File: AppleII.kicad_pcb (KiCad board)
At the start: 2 copper layers, 215.5 x 361.2 mm, 201 parts, among them J0 Cassette Data In, J1 74LS257, J13 74LS74, J14 GAME_IO_Conn, J18 Aux Video, J2 Cassette Data Out, J3 Conn_01x16, J4 Conn_01x25, J5 Conn_01x25, J6 Conn_01x24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

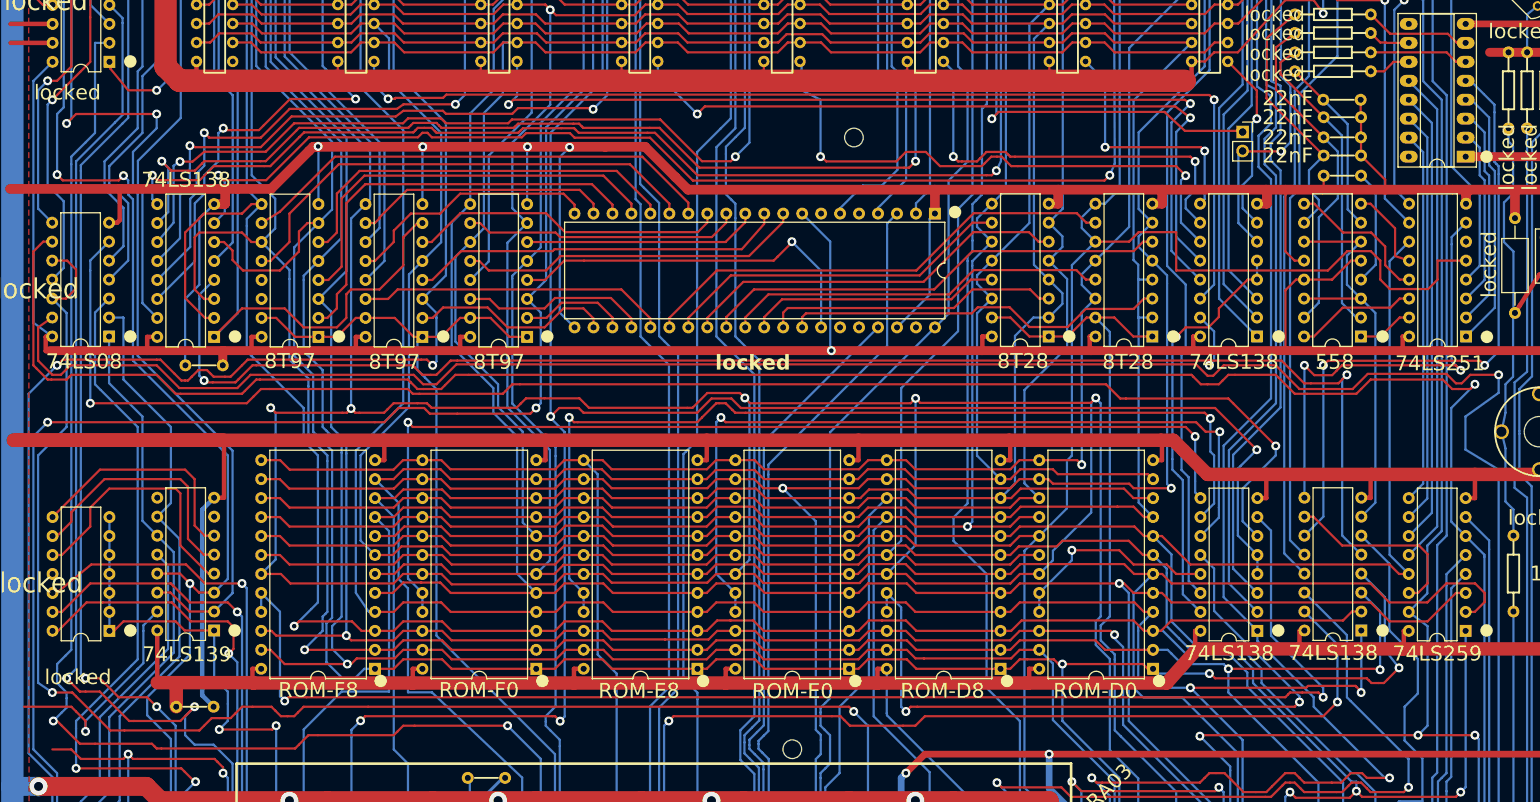
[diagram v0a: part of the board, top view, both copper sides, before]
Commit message: add missing test points
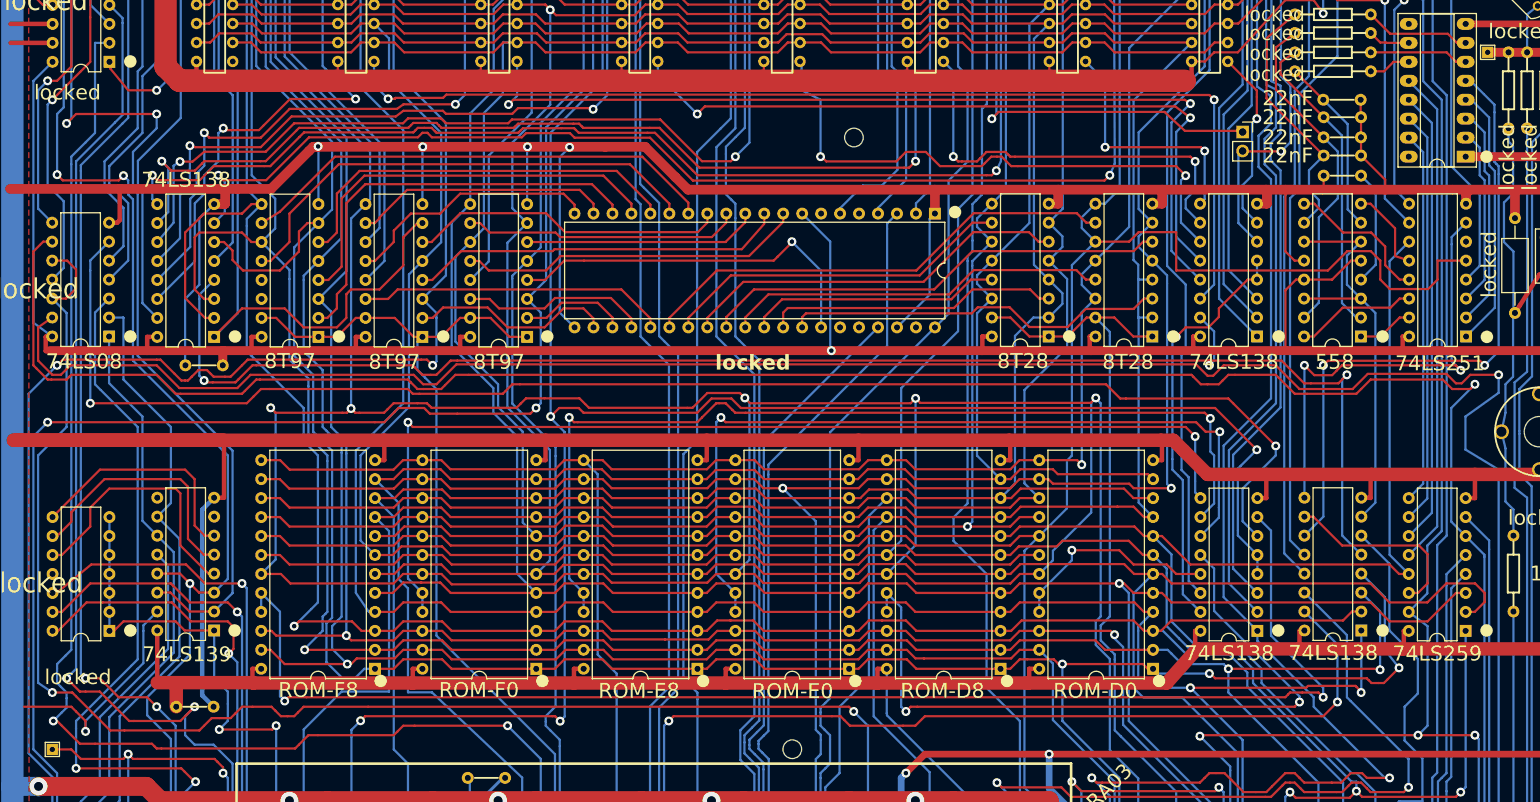
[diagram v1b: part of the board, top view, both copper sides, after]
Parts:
- added TP1: TestPoint, TestPoint:TestPoint_THTPad_1.5x1.5mm_Drill0.7mm, F.Cu at (50.9, 187.6)
- added TP2: TestPoint, TestPoint:TestPoint_THTPad_1.5x1.5mm_Drill0.7mm, F.Cu at (243.1, 94.2)
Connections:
- net /Address Decoder and Onboard IO/KBD_Data0 renamed /Address Decoder and Onboard IO/KBD0
- net /Address Decoder and Onboard IO/KBD_Data1 renamed /Address Decoder and Onboard IO/KBD1
- net /Address Decoder and Onboard IO/KBD_Data2 renamed /Address Decoder and Onboard IO/KBD2
- net /Address Decoder and Onboard IO/KBD_Data3 renamed /Address Decoder and Onboard IO/KBD3
- net /Address Decoder and Onboard IO/KBD_Data4 renamed /Address Decoder and Onboard IO/KBD4
- net /Address Decoder and Onboard IO/KBD_Data5 renamed /Address Decoder and Onboard IO/KBD5
- net /Address Decoder and Onboard IO/KBD_Data6 renamed /Address Decoder and Onboard IO/KBD6
- net H0 renamed /Clock Generation/H0
- net H1 renamed /Clock Generation/H1
- net H2 renamed /Clock Generation/H2
- net H3 renamed /Clock Generation/H3
- net H4 renamed /Clock Generation/H4
- net H5 renamed /Clock Generation/H5
- net V1 renamed /Clock Generation/V1
- net V2 renamed /Clock Generation/V2
- net V3 renamed /Clock Generation/V3
- net V4 renamed /Clock Generation/V4

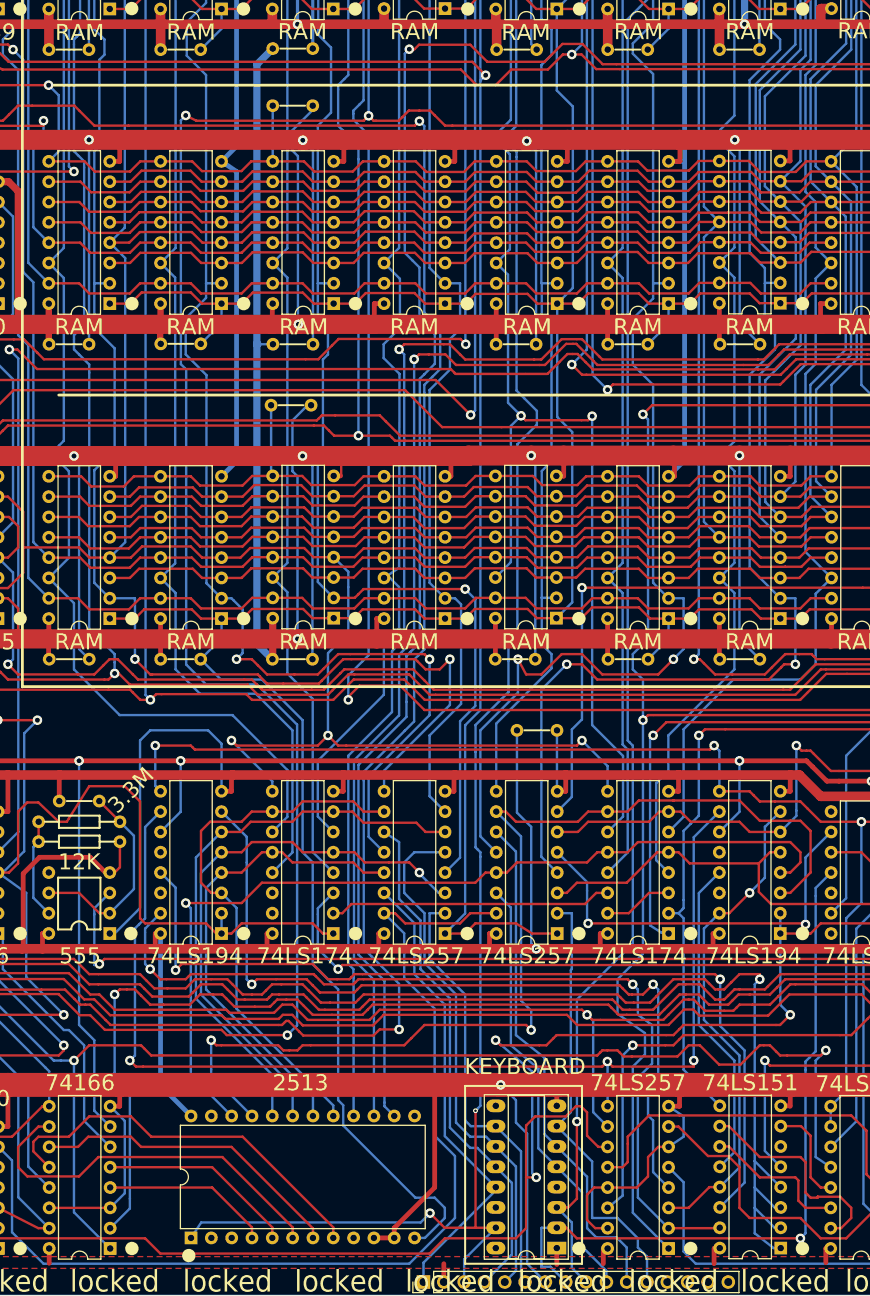
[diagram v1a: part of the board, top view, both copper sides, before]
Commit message: add alternative char gen footprint
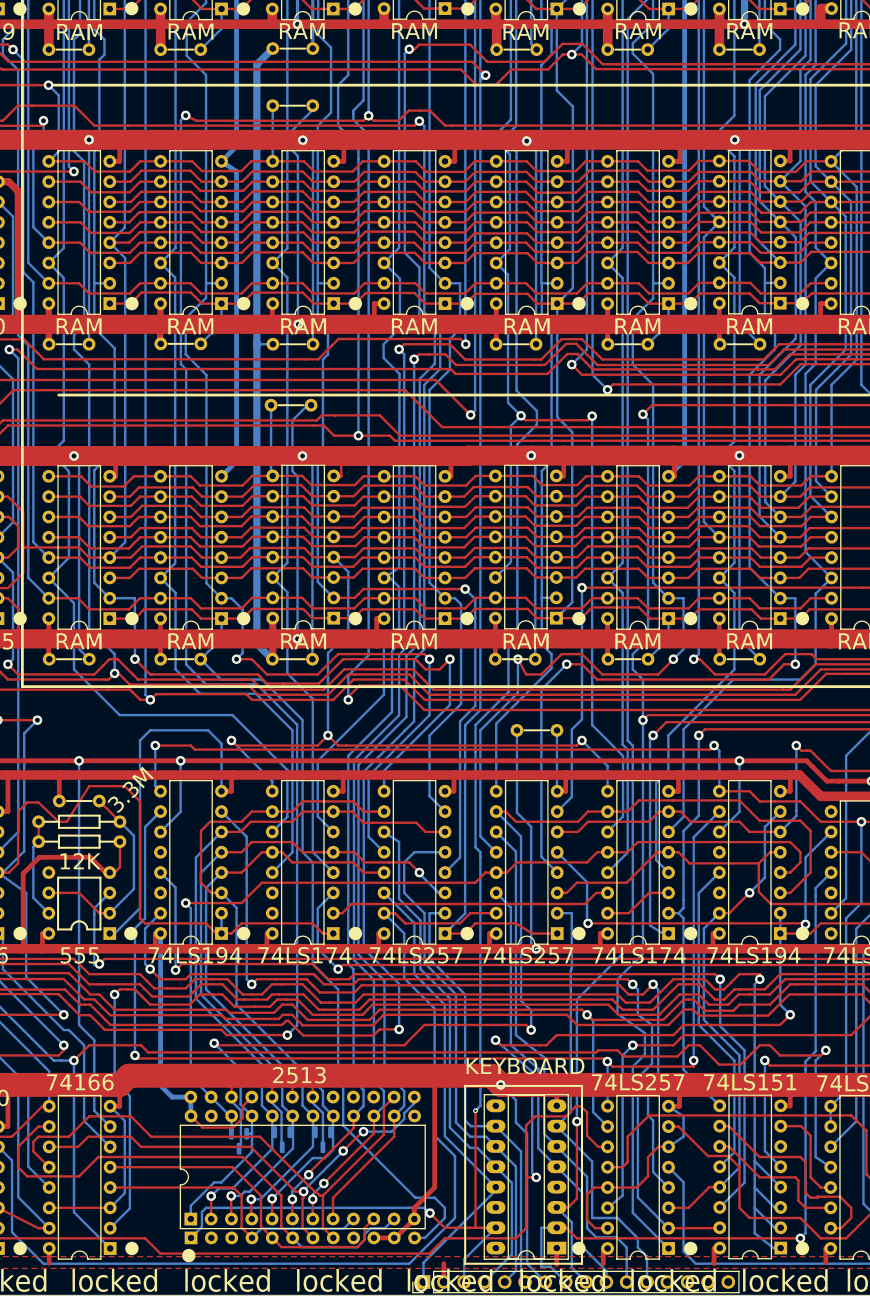
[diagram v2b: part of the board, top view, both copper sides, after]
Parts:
- added Aalt5: 2513->2716, Package_DIP:DIP-24_W15.24mm_Socket, F.Cu at (96.6, 366.1)
- added D21: BAT54A, Package_TO_SOT_SMD:SOT-23, B.Cu at (108.1, 356.2)
- added D22: BAT54A, Package_TO_SOT_SMD:SOT-23, B.Cu at (113.2, 356.2)
- added D23: BAT54A, Package_TO_SOT_SMD:SOT-23, B.Cu at (102.7, 356.4)
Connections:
- net LD0 renamed /CPU Tranceiver Driver and Data MUX/LD0
- net LD1 renamed /CPU Tranceiver Driver and Data MUX/LD1
- net LD2 renamed /CPU Tranceiver Driver and Data MUX/LD2
- net LD3 renamed /CPU Tranceiver Driver and Data MUX/LD3
- net LD4 renamed /CPU Tranceiver Driver and Data MUX/LD4
- net LD5 renamed /CPU Tranceiver Driver and Data MUX/LD5
- net LD6 renamed /CPU Tranceiver Driver and Data MUX/LD6
- net LD7 renamed /CPU Tranceiver Driver and Data MUX/LD7
- net Net-(A3-C) renamed /Video Generation/O1
- net Net-(A3-D) renamed /Video Generation/O2
- net Net-(A3-E) renamed /Video Generation/O3
- net Net-(A3-F) renamed /Video Generation/O4
- net Net-(A3-G) renamed /Video Generation/O5
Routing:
- net GND: track 3190.9 -> 3223.2 mm
- net /Video Generation/O4: track 39.4 -> 61.2 mm, vias 0 -> 3
- net /CPU Tranceiver Driver and Data MUX/LD2: track 69.9 -> 87.6 mm, vias 1 -> 2
- net /Video Generation/O5: track 49.9 -> 67.4 mm
- net /CPU Tranceiver Driver and Data MUX/LD3: track 70.8 -> 88.2 mm, vias 0 -> 1
- net VB: track 228.9 -> 246.0 mm, vias 3 -> 5
- net VC: track 757.8 -> 774.9 mm, vias 4 -> 6
- net VA: track 311.4 -> 328.5 mm
- net /Video Generation/O2: track 24.7 -> 41.7 mm
- net /CPU Tranceiver Driver and Data MUX/LD0: track 68.2 -> 85.1 mm, vias 0 -> 1
- net /CPU Tranceiver Driver and Data MUX/LD1: track 59.2 -> 76.0 mm, vias 0 -> 1
- net /Video Generation/O3: track 48.2 -> 64.7 mm
- net /CPU Tranceiver Driver and Data MUX/LD4: track 135.4 -> 151.0 mm
- net /Video Generation/O1: track 21.1 -> 36.3 mm
- net +5V: track 2065.7 -> 2077.7 mm
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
